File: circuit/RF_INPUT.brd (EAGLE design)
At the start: 100 x 80 mm, 90 parts, among them IC1 TS464, IC2 SN74LVC1G3157DBVR, U1 SA612, U2 SA612, U3 SA612, X1 BU-SMA-V, X4 SMA-142-0701-801/806, X5 BU-SMA-V, X6 SMA-142-0701-801/806

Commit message: - развели половину
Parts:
- removed C37: nc, rcl:C0603
- removed R10: 680K, rcl:R0603
- C1, C10, C11, C15, C18, C19, C20, C21, C22, C23, C26, C31, C32, C33, C34, C4, C6, C7, C8: device rcl:C0603 -> rcl:C0805
- C24: value 220N -> 100N
- C25: value nc -> 220N; device rcl:C0603 -> rcl:C0805
- R11: value 680K -> 330K
- R41: value 150K -> 330k
- moved C19 154.5 mm to (85.1, 37.5)
- moved C6 151.1 mm to (81.9, 22.2)
- moved R41 151.0 mm to (67.9, 21.0)
- moved R5 145.4 mm to (79.4, 16.5)
- moved R38 144.9 mm to (63.5, 51.4)
- moved R24 144.3 mm to (76.2, 29.2)
- moved R30 143.9 mm to (57.1, 29.2)
- moved R39 141.0 mm to (63.5, 47.6)
- moved R29 134.0 mm to (74.9, 20.3)
- moved C24 125.4 mm to (84.5, 27.9)
- moved R3 125.2 mm to (47.6, 39.4)
- moved R35 122.8 mm to (27.9, 7.62), turned to 270 degrees
- moved C33 120.6 mm to (24.8, 6.99), turned to 90 degrees
- moved C31 118.4 mm to (31.8, 8.26), turned to 180 degrees
- moved R4 115.7 mm to (37.5, 43.8), turned to 270 degrees
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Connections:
- removed net LO_RX: U3.6
- new net N$3: C25.2, U3.6
- net +6V0: no longer R10.2
- net GND: now also C24.1; no longer C24.2, C25.2, C37.2, R11.2
- net LO_TX: now also C25.1
- net N$47: no longer C37.1
- net N$59: no longer C25.1
- net N$73: no longer R10.1
- net OPA_BIAS: now also C24.2, R11.2; no longer C24.1
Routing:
- net GND: track 0.00 -> 179.3 mm, vias 0 -> 2
- net LO_TX: track 0.00 -> 63.9 mm
- net N$5: track 0.00 -> 21.8 mm
- net +6V0: track 0.00 -> 16.6 mm
- net RF_DDS: track 0.00 -> 16.5 mm
- net N$37: track 0.00 -> 14.9 mm
- net N$53: track 0.00 -> 12.6 mm
- net N$63: track 0.00 -> 10.4 mm
- net N$30: track 0.00 -> 8.54 mm
- net N$1: track 0.00 -> 8.47 mm
- net N$60: track 0.00 -> 7.70 mm
- net N$61: track 0.00 -> 7.66 mm
- net N$35: track 0.00 -> 7.20 mm
- net N$76: track 0.00 -> 6.95 mm
- net N$42: track 0.00 -> 6.94 mm
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
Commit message: - почти разведенная схема
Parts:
- added Q1, Q2: IRML6302, transistor-small-signal:SOT23
- added R10, R42: 4.7k, rcl:R0603
- added R43, R44: 68k, rcl:R0603
- added R45: 220, rcl:R0603
- added X8: (no value), con-phoenix-254:2POL254
- C30: device rcl:C0603 -> rcl:C0805
- R14, R19, R2, R21, R3: device rcl:R0603 -> rcl:R0805
- moved R8 105.0 mm to (57.1, 50.2), turned to 90 degrees
- moved C13 104.2 mm to (80.0, 67.3), turned to 270 degrees
- moved R11 95.9 mm to (52.7, 69.2)
- moved X3 93.8 mm to (76.2, 67.3), turned to 270 degrees
- moved R37 89.3 mm to (69.2, 54.6), turned to 270 degrees
- moved C9 88.0 mm to (63.5, 67.3), turned to 270 degrees
- moved R28 78.2 mm to (59.7, 67.3), turned to 270 degrees
- moved C36 75.3 mm to (57.1, 71.8), turned to 90 degrees
- moved C35 61.1 mm to (48.3, 73.7)
- moved R38 50.8 mm to (36.8, 8.26)
- moved R29 50.2 mm to (57.1, 67.3), turned to 90 degrees
- moved R39 50.2 mm to (36.8, 5.08)
- moved R5 47.0 mm to (50.2, 53.3), turned to 270 degrees
- moved C6 42.7 mm to (52.7, 53.3), turned to 90 degrees
- moved R30 42.6 mm to (59.7, 71.8), turned to 90 degrees
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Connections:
- new net N$10: R10.1, X8.1
- new net N$11: IC2.1, R45.2
- new net N$4: C26.1, C27.1, Q2.3, U3.8
- new net N$6: Q1.1, R10.2, R43.2
- new net N$7: Q2.1, R42.2, R44.2
- new net N$8: C15.1, C16.1, Q1.3, U2.8
- new net N$9: R42.1, X8.2
- net +6V0: now also Q1.2, Q2.2, R43.1, R44.1; no longer C15.1, C16.1, C26.1, C27.1, U2.8, U3.8
- net ADC_SWITCH_CNTRL: now also IC2.4; no longer R36.2
- net ADC_SWITCH_NC: now also IC1.1, R45.1; no longer IC1.7, IC2.1
- net ADC_SWITCH_NO: now also R36.1; no longer IC2.3
- net ADC_SWITCH_NO2: now also IC1.7; no longer IC1.1
- net N$2: now also IC2.3, R36.2; no longer IC2.4, R36.1
- net N$55: now also IC1.2; no longer IC1.6
- net N$59: now also IC1.3; no longer IC1.5
- net N$69: now also IC1.6; no longer IC1.2
- net N$73: now also IC1.5; no longer IC1.3
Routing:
- net +6V0: track 16.6 -> 199.7 mm, vias 0 -> 2
- net GND: track 179.3 -> 350.2 mm, vias 2 -> 6
- net N$41: track 0.00 -> 79.5 mm, vias 0 -> 2
- net N$73: track 0.00 -> 71.2 mm, vias 0 -> 2
- net N$47: track 0.00 -> 69.4 mm, vias 0 -> 2
- net N$69: track 0.00 -> 56.5 mm, vias 0 -> 2
- net N$59: track 0.00 -> 36.8 mm, vias 0 -> 2
- net N$11: track 0.00 -> 36.5 mm, vias 0 -> 2
- net OPA_BIAS: track 0.00 -> 25.0 mm
- net N$4: track 0.00 -> 20.7 mm, vias 0 -> 2
- net N$55: track 0.00 -> 17.9 mm, vias 0 -> 2
- net ADC_SWITCH_NO2: track 0.00 -> 11.5 mm
- net N$8: track 0.00 -> 11.1 mm
- net ADC_SWITCH_NC: track 0.00 -> 10.5 mm
- net ADC_SWITCH_NO: track 0.00 -> 8.57 mm
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
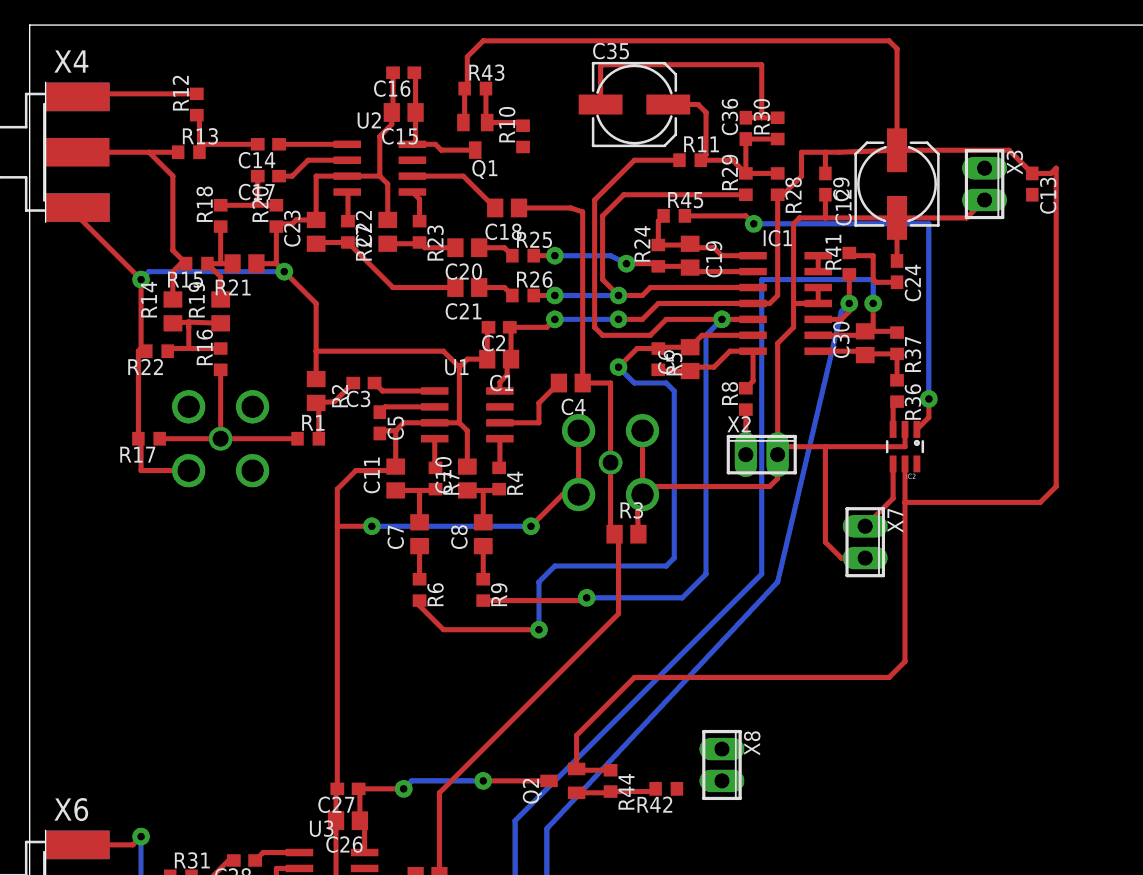
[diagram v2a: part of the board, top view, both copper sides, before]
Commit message: - добавили транзистор, чтобы переключалось одной линией. - индуктивность на питание
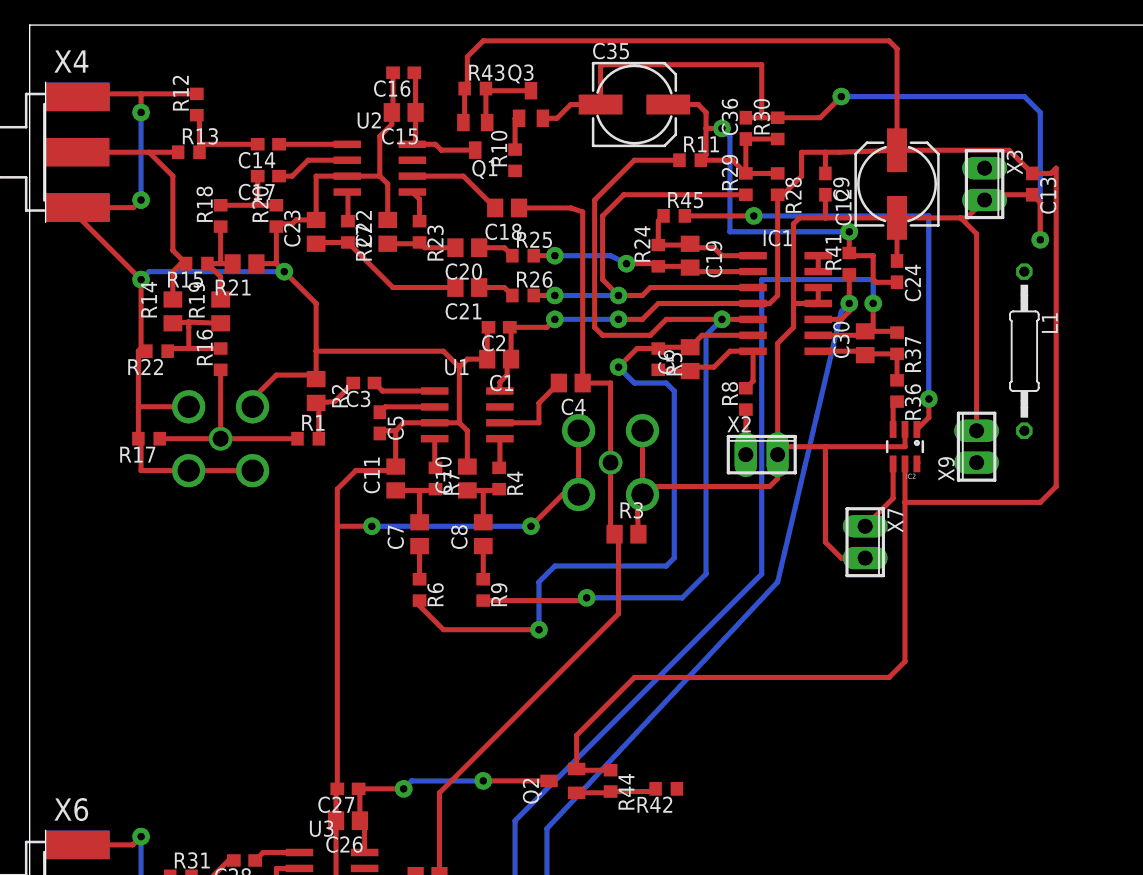
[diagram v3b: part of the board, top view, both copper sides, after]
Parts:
- removed X8: (no value), con-phoenix-254:2POL254
- added L1: 100u, rcl:0207/12
- added Q3: 2N7002, transistor-small-signal:SOT23
- added X9: (no value), con-phoenix-254:2POL254
- C12: value 33u -> 220u
- moved R10 2.01 mm to (38.7, 69.2)
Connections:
- net ADC_SWITCH_CNTRL renamed N$12
- removed net ADC_SWITCH_COMM: IC2.6
- removed net N$10: R10.1, X8.1
- new net N$14: Q3.1, R10.2
- new net SET_CHANNEL: IC2.6, Q2.1, R10.1, R42.2, R44.2
- net +6V0: now also L1.2; no longer X3.1
- net GND: now also Q3.2, X9.2
- net N$6: now also Q3.3; no longer R10.2
- net N$7: now also L1.1, X3.1; no longer Q2.1, R42.2, R44.2
- net N$9: now also X9.1; no longer X8.2
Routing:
- net GND: track 350.2 -> 442.4 mm, vias 6 -> 10
- net OPA_BIAS: track 25.0 -> 46.0 mm, vias 0 -> 2
- net SET_CHANNEL: track 0.00 -> 6.58 mm
- net N$7: track 6.44 -> 0.00 mm
- net N$14: track 0.00 -> 2.82 mm
- net N$6: track 5.71 -> 6.52 mm

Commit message: - немного компактифицировали
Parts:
- moved C4 33.2 mm to (19.1, 28.6)
- moved R4 30.1 mm to (10.8, 29.8)
- moved C8 27.8 mm to (11.4, 26.7), turned to 180 degrees
- moved C10 27.0 mm to (10.2, 33.0), turned to 0 degrees
- moved C7 25.9 mm to (6.35, 31.8)
- moved R6 25.9 mm to (6.35, 27.3)
- moved C1 25.6 mm to (20.3, 34.3)
- moved C2 25.6 mm to (20.3, 36.8)
- moved U1 24.9 mm to (15.2, 33.7), turned to 180 degrees
- moved C11 23.7 mm to (6.99, 35.6), turned to 180 degrees
- moved R7 22.9 mm to (10.8, 36.2)
- moved R9 22.5 mm to (15.2, 26.7), turned to 0 degrees
- moved R3 20.4 mm to (27.3, 41.3), turned to 180 degrees
- moved C19 19.5 mm to (46.4, 43.2)
- moved C24 19.3 mm to (63.5, 41.9)
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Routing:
- net N$47: track 69.4 -> 0.00 mm, vias 2 -> 0
- net N$69: track 56.5 -> 6.29 mm, vias 2 -> 0
- net GND: track 442.4 -> 410.8 mm
- net +6V0: track 199.7 -> 228.5 mm
- net N$59: track 36.8 -> 53.7 mm
- net N$41: track 79.5 -> 63.2 mm
- net N$73: track 71.2 -> 57.5 mm
- net N$55: track 17.9 -> 28.8 mm
- net N$53: track 12.6 -> 7.48 mm
- net N$4: track 20.7 -> 16.2 mm
- net N$9: track 0.00 -> 4.14 mm
- net N$7: track 0.00 -> 3.18 mm
- net N$65: track 5.13 -> 7.76 mm
- net N$11: track 36.9 -> 34.4 mm
- net N$61: track 7.66 -> 5.23 mm
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
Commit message: - развели вчерновую
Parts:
- moved X3 33.7 mm to (47.0, 73.0)
- moved C13 22.8 mm to (54.6, 60.3), turned to 180 degrees
- moved L1 18.8 mm to (54.0, 68.6), turned to 270 degrees
- moved X9 10.8 mm to (62.9, 19.7), turned to 270 degrees
- moved X7 7.65 mm to (55.9, 26.0), turned to 180 degrees
- moved R29 5.68 mm to (46.4, 51.4)
- moved R45 5.68 mm to (43.2, 48.9)
- moved R28 5.12 mm to (49.5, 51.4)
- moved C24 4.58 mm to (59.7, 44.5)
- moved R11 4.58 mm to (43.2, 53.3)
- moved C12 4.58 mm to (59.7, 51.4)
- moved C30 4.58 mm to (57.1, 38.7)
- moved C35 4.58 mm to (47.6, 63.5)
- moved C36 4.58 mm to (47.6, 55.9)
- moved IC1 4.58 mm to (50.8, 41.9)
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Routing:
- net SET_CHANNEL: track 6.28 -> 80.6 mm, vias 0 -> 4
- net N$47: track 0.00 -> 51.1 mm, vias 0 -> 2
- net N$69: track 6.29 -> 50.7 mm, vias 0 -> 2
- net GND: track 410.8 -> 401.3 mm, vias 10 -> 12
- net +6V0: track 228.5 -> 219.4 mm
- net N$59: track 53.7 -> 47.1 mm
- net N$55: track 28.8 -> 24.1 mm
- net N$7: track 3.18 -> 7.25 mm
- net N$71: track 2.64 -> 0.00 mm
- net N$73: track 57.5 -> 55.1 mm
- net N$11: track 34.4 -> 35.6 mm
- net OPA_BIAS: track 47.7 -> 46.6 mm
- net N$5: track 21.7 -> 20.7 mm
- net N$12: track 5.90 -> 5.11 mm
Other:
- board size 100 x 80 mm -> 68.9 x 80 mm

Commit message: - вроде готовая плата
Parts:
- moved X9 5.08 mm to (57.8, 19.7), turned to 180 degrees
- moved C18 4.62 mm to (29.8, 63.5)
- moved C20 4.49 mm to (24.8, 59.1), turned to 90 degrees
- moved R42 3.86 mm to (59.1, 24.1), turned to 90 degrees
- moved R27 3.86 mm to (21.6, 64.1)
- moved U2 3.81 mm to (24.1, 68.6)
- moved C15 3.81 mm to (26.0, 73.0)
- moved C16 3.81 mm to (26.0, 76.2)
- moved C22 3.81 mm to (24.8, 63.5)
- moved R23 3.81 mm to (27.3, 63.5)
- moved R25 3.81 mm to (27.3, 57.1), turned to 270 degrees
- moved R26 3.24 mm to (22.9, 54.6)
- moved C19 3.18 mm to (39.4, 45.7)
- moved C6 3.18 mm to (39.4, 38.1)
- moved C9 3.18 mm to (50.8, 51.4)
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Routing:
- net GND: track 401.3 -> 412.9 mm, vias 12 -> 14
- net LO_TX: track 66.1 -> 60.0 mm
- net N$41: track 63.5 -> 58.6 mm
- net +6V0: track 219.4 -> 215.9 mm
- net N$59: track 47.1 -> 50.0 mm
- net N$55: track 24.1 -> 26.8 mm
- net N$53: track 7.48 -> 4.81 mm
- net N$71: track 0.00 -> 2.64 mm
- net N$39: track 5.97 -> 3.80 mm
- net N$60: track 7.70 -> 5.55 mm
- net N$69: track 50.7 -> 48.6 mm
- net N$47: track 51.1 -> 49.0 mm
- net N$63: track 10.4 -> 8.85 mm
- net N$8: track 11.1 -> 12.5 mm
- net N$61: track 5.23 -> 6.61 mm
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- added copper zone on layer 1, net GND
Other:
- board size 68.9 x 80 mm -> 64.4 x 80 mm
